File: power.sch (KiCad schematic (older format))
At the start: 6 parts, among them U401 7805, U402 LF33CDT-TRY

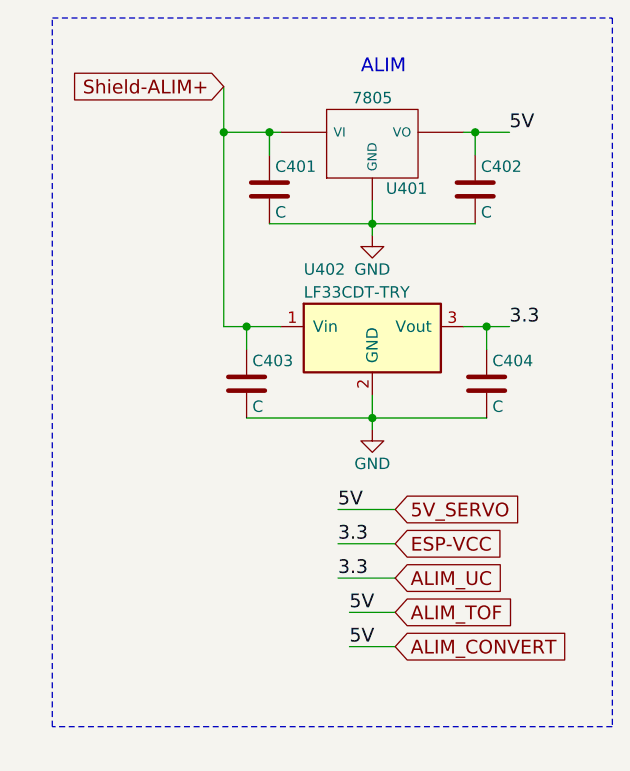
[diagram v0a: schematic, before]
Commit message: finish schematics. add componants, find right chip, firest verification OK, ready for routing
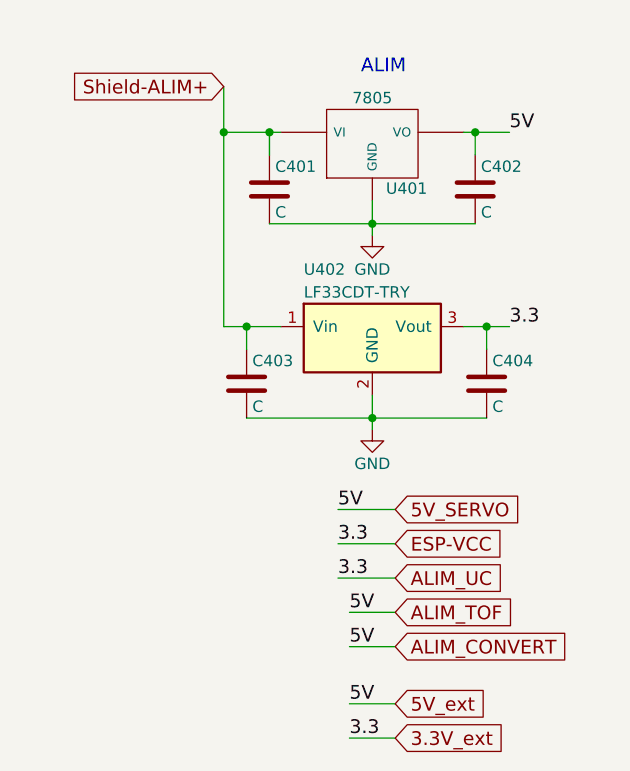
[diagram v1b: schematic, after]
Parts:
- C401, C402, C403, C404: footprint (none) -> Capacitors_THT:C_Disc_D3.8mm_W2.6mm_P2.50mm
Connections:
- net ALIM_UC renamed 3.3V_ext
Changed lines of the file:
@@
 ALIM
 $Comp
-L GND #PWR013
+L GND #PWR017
 U 1 1 5A7A449C
 P 2600 2550
-F 0 "#PWR013" H 2600 2300 50  0001 C CNN
+F 0 "#PWR017" H 2600 2300 50  0001 C CNN
 F 1 "GND" H 2600 2400 50  0000 C CNN
 F 2 "" H 2600 2550 50  0001 C CNN
@@
 F 0 "C402" H 3075 2450 50  0000 L CNN
 F 1 "C" H 3075 2250 50  0000 L CNN
-F 2 "" H 3088 2200 50  0001 C CNN
+F 2 "Capacitors_THT:C_Disc_D3.8mm_W2.6mm_P2.50mm" H 3088 2200 50  0001 C CNN
 F 3 "" H 3050 2350 50  0001 C CNN
 	1    3050 2350
@@
 F 0 "C401" H 2175 2450 50  0000 L CNN
 F 1 "C" H 2175 2250 50  0000 L CNN
-F 2 "" H 2188 2200 50  0001 C CNN
+F 2 "Capacitors_THT:C_Disc_D3.8mm_W2.6mm_P2.50mm" H 2188 2200 50  0001 C CNN
 F 3 "" H 2150 2350 50  0001 C CNN
 	1    2150 2350
@@
 3.3
 $Comp
-L GND #PWR014
+L GND #PWR018
 U 1 1 5A7A44C6
 P 2600 3400
-F 0 "#PWR014" H 2600 3150 50  0001 C CNN
+F 0 "#PWR018" H 2600 3150 50  0001 C CNN
 F 1 "GND" H 2600 3250 50  0000 C CNN
 F 2 "" H 2600 3400 50  0001 C CNN
@@
 F 0 "C404" H 3125 3300 50  0000 L CNN
 F 1 "C" H 3125 3100 50  0000 L CNN
-F 2 "" H 3138 3050 50  0001 C CNN
+F 2 "Capacitors_THT:C_Disc_D3.8mm_W2.6mm_P2.50mm" H 3138 3050 50  0001 C CNN
 F 3 "" H 3100 3200 50  0001 C CNN
 	1    3100 3200
@@
 F 0 "C403" H 2075 3300 50  0000 L CNN
 F 1 "C" H 2075 3100 50  0000 L CNN
-F 2 "" H 2088 3050 50  0001 C CNN
+F 2 "Capacitors_THT:C_Disc_D3.8mm_W2.6mm_P2.50mm" H 2088 3050 50  0001 C CNN
 F 3 "" H 2050 3200 50  0001 C CNN
 	1    2050 3200
@@
 	2600 3250 2600 3400
 Connection ~ 2600 3350
-Wire Notes Line
-	1200 1600 3650 1600
-Wire Notes Line
-	3650 1600 3650 4700
-Wire Notes Line
-	3650 4700 1200 4700
-Wire Notes Line
-	1200 4700 1200 1600
 Text GLabel 2700 3750 2    60   Input ~ 0
 5V_SERVO
@@
 Wire Wire Line
 	2450 4050 2700 4050
+Text GLabel 2700 4600 2    60   Input ~ 0
+5V_ext
+Text GLabel 2700 4750 2    60   Input ~ 0
+3.3V_ext
+Text Label 2500 4600 0    60   ~ 0
+5V
+Text Label 2500 4750 0    60   ~ 0
+3.3
+Wire Wire Line
+	2500 4750 2700 4750
+Wire Wire Line
+	2500 4600 2700 4600
 $EndSCHEMATC
